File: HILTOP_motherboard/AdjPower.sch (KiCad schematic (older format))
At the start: 92 parts, among them Q1 Q_NMOS_DS_POWERPAK, Q2 Q_NMOS_DS_POWERPAK, Q4 2N7002, U10 TLC271, U11 ADS1015, U12 MCP4725, U8 LM5118, U9 INA250A3

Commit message: Furthe progress on Schematics, assigned all main footprints using latest libraries, removed unwanted tracking and parts from original PCB layout
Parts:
- C111, C115, C184, C185, C193, C194, C63, C64, C69: footprint Capacitors_SMD:C_0805 -> Capacitor_SMD:C_0805_2012Metric
- C112, C117, C118, C180, C187, C188, C189, C190, C191, C192, C57, C60, C61, C62: footprint Capacitors_SMD:C_0603 -> Capacitor_SMD:C_0603_1608Metric
- C179, C56, C58: footprint Capacitors_SMD:C_1206 -> Capacitor_SMD:C_1206_3216Metric
- C181, C182, C183, C65: footprint Capacitors_SMD:C_1210 -> Capacitor_SMD:C_1210_3225Metric
- C186, C67: footprint Capacitors_SMD:CP_Elec_6.3x7.7 -> Capacitor_SMD:CP_Elec_6.3x7.7
- C54: footprint Capacitors_SMD:C_0603 -> Capacitor_SMD:C_0201_0603Metric
- C70, C79: renamed from C?; footprint Capacitors_SMD:CP_Elec_6.3x7.7 -> Capacitor_SMD:CP_Elec_6.3x7.7
- D10, D19, D7, D8, D9, Q4: footprint TO_SOT_Packages_SMD:SOT-23 -> Package_TO_SOT_SMD:SOT-23
- D5: footprint KiCAD_PCB_Lib:TO-263AB -> Devtank_PCB_Lib:TO-263AB
- D6: footprint KiCAD_PCB_Lib:DPAK -> Devtank_PCB_Lib:DPAK
- L4: footprint KiCAD_PCB_Lib:Inductor_Coilcraft_SER2800 -> Devtank_PCB_Lib:Inductor_Coilcraft_SER2800
- Q1, Q2: footprint KiCAD_PCB_Lib:PowerPAK_SO-8 -> Devtank_PCB_Lib:PowerPAK_SO-8
- R105, R112, R113, R114, R115, R116, R117, R118, R123, R132, R133, R142, R143, R165, R166, R57, R58, R59, R60, R61, R62, R64, R74, R75, R76: footprint Resistors_SMD:R_0603 -> Resistor_SMD:R_0603_1608Metric
- R63: footprint Resistors_SMD:R_1206 -> Resistor_SMD:R_1206_3216Metric
- R65, R66, R67, R68: footprint Resistors_SMD:R_0603 -> Resistor_SMD:R_0603_1608Metric_Pad0.84x1.00mm_HandSolder
- R69: footprint KiCAD_PCB_Lib:RL7520W_3008 -> Devtank_PCB_Lib:RL7520W_3008
- RL1: footprint KiCAD_PCB_Lib:Relay_SPST_TE_PCH -> Devtank_PCB_Lib:Relay_SPST_TE_PCH
- TP1, TP2, TP3, TP4, TP5, TP6, TP7: footprint Measurement_Points:Measurement_Point_Round-TH_Small -> TestPoint:TestPoint_THTPad_D1.5mm_Drill0.7mm
- U10: footprint Housings_SOIC:SOIC-8_3.9x4.9mm_Pitch1.27mm -> Package_SOIC:SOIC-8_3.9x4.9mm_P1.27mm
- U11: footprint Housings_SSOP:TSSOP-10_3x3mm_Pitch0.5mm -> Package_SSOP:TSSOP-10_3x3mm_P0.5mm
- U12: footprint TO_SOT_Packages_SMD:SOT-23-6 -> Package_TO_SOT_SMD:SOT-23-6
- U8: footprint Housings_SSOP:HTSSOP-20-1EP_4.4x6.5mm_Pitch0.65mm_ThermalPad -> Package_SSOP:HTSSOP-20-1EP_4.4x6.5mm_P0.65mm_ThermalPad
- U9: footprint Housings_SSOP:TSSOP-16_4.4x5mm_Pitch0.65mm -> Package_SSOP:TSSOP-16_4.4x5mm_P0.65mm
- W1: footprint Measurement_Points:Measurement_Point_Round-TH_Small -> TestPoint:TestPoint_THTPad_1.5x1.5mm_Drill0.7mm

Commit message: Schematics complete - 1st draft
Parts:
- C111, C112, C115, C117, C118, C179, C180, C181, C182, C183, C184, C185, C187, C188, C189, C190, C191, C192, C193, C194, C54, C56, C57, C58, C60, C61, C62, C63, C64, C65, C69: symbol C -> device:C
- C186, C67, C70, C79: symbol CP -> device:CP
- D10, D7, D8, D9: symbol D_x2_Serial_AKC -> device:D_x2_Serial_AKC
- D19: symbol D_Schottky -> device:D_Schottky
- D20: symbol D -> device:D
- D5: symbol D_Schottky_x2_KCom_AAK -> device:D_Schottky_x2_KCom_AAK
- D6: symbol D_Schottky_x2_KCom_AKA -> device:D_Schottky_x2_KCom_AKA
- L4: symbol L -> device:L
- Q1, Q2: symbol Q_NMOS_DS_POWERPAK -> Devtank:Q_NMOS_DS_POWERPAK
- Q4: symbol 2N7002 -> Transistor:2N7002
- R105, R112, R113, R114, R115, R116, R117, R118, R123, R132, R133, R142, R143, R165, R166, R57, R58, R59, R60, R61, R62, R63, R64, R65, R66, R67, R68, R69, R74, R75, R76: symbol R -> device:R
- RL1: symbol SPST-NO -> Devtank:SPST-NO
- TP1, TP2, TP3, TP4, TP5, TP6, TP7: footprint TestPoint:TestPoint_THTPad_D1.5mm_Drill0.7mm -> TestPoint:TestPoint_THTPad_D1.0mm_Drill0.5mm; symbol TEST_1P -> HILTOP_Motherboard-rescue:TEST_1P
- U10: symbol TLC271 -> Devtank:TLC271
- U11: symbol ADS1015 -> Devtank:ADS1015
- U12: symbol MCP4725 -> Devtank:MCP4725
- U8: symbol LM5118 -> Devtank:LM5118
- U9: symbol INA250 -> Devtank:INA250
- W1: symbol TEST_1P -> HILTOP_Motherboard-rescue:TEST_1P
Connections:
- net labels removed: PSU_ADC_ADDR, PSU_ALERT_RDY, PSU_DAC_ADDR
- wire segments 306 -> 418

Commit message: BOM nearly complete!
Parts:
- removed W1: TP, TestPoint:TestPoint_THTPad_1.5x1.5mm_Drill0.7mm, symbol HILTOP_Motherboard-rescue:TEST_1P
- added TP95: TP, TestPoint:TestPoint_THTPad_D1.0mm_Drill0.5mm, symbol HILTOP_Motherboard-rescue:TEST_1P
- Q1, Q2: value Q_NMOS_DS_POWERPAK -> Si7148DP-T1-E3
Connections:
- net at U8.11 (SYNC): now also TP95.1
- no-connect marks 0 -> 3
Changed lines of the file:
@@
 $Descr A3 16535 11693
 encoding utf-8
-Sheet 7 12
+Sheet 6 12
 Title "HILTOP Motherboard"
 Date "26th January 2018"
@@
 $EndComp
 $Comp
-L HILTOP_Motherboard-rescue:TEST_1P W1
-U 1 1 58E90AB1
-P 5550 4850
-F 0 "W1" H 5550 5120 50  0000 C CNN
-F 1 "TP" H 5550 5050 50  0000 C CNN
-F 2 "TestPoint:TestPoint_THTPad_1.5x1.5mm_Drill0.7mm" H 5750 4850 50  0001 C CNN
-F 3 "" H 5750 4850 50  0000 C CNN
-	1    5550 4850
-	-1   0    0    1
-$EndComp
-$Comp
 L device:C C64
 U 1 1 58E9153E
@@
 P 6800 3100
 F 0 "Q1" H 7000 3150 50  0000 L CNN
-F 1 "Q_NMOS_DS_POWERPAK" H 7000 3050 50  0000 L CNN
+F 1 "Si7148DP-T1-E3" H 7000 3050 50  0000 L CNN
 F 2 "Devtank_PCB_Lib:PowerPAK_SO-8" H 7000 3200 50  0001 C CNN
 F 3 "" H 6800 3100 50  0000 C CNN
@@
 P 7350 5000
 F 0 "Q2" H 7550 5050 50  0000 L CNN
-F 1 "Q_NMOS_DS_POWERPAK" H 7550 4950 50  0000 L CNN
+F 1 "Si7148DP-T1-E3" H 7550 4950 50  0000 L CNN
 F 2 "Devtank_PCB_Lib:PowerPAK_SO-8" H 7550 5100 50  0001 C CNN
 F 3 "" H 7350 5000 50  0000 C CNN
@@
 Wire Wire Line
 	9400 6300 9600 6300
+NoConn ~ 15100 4800
+NoConn ~ 8550 8500
+NoConn ~ 8450 8550
+$Comp
+L HILTOP_Motherboard-rescue:TEST_1P TP?
+U 1 1 5CBFAD8E
+P 5550 4850
+AR Path="/5CBFAD8E" Ref="TP?"  Part="1"
+AR Path="/589A1BA0/5CBFAD8E" Ref="TP95"  Part="1"
+F 0 "TP95" H 5550 5100 50  0000 C CNN
+F 1 "TP" H 5550 5050 50  0001 C CNN
+F 2 "TestPoint:TestPoint_THTPad_D1.0mm_Drill0.5mm" H 5750 4850 50  0001 C CNN
+F 3 "" H 5750 4850 50  0000 C CNN
+	1    5550 4850
+	-1   0    0    1
+$EndComp
 $EndSCHEMATC

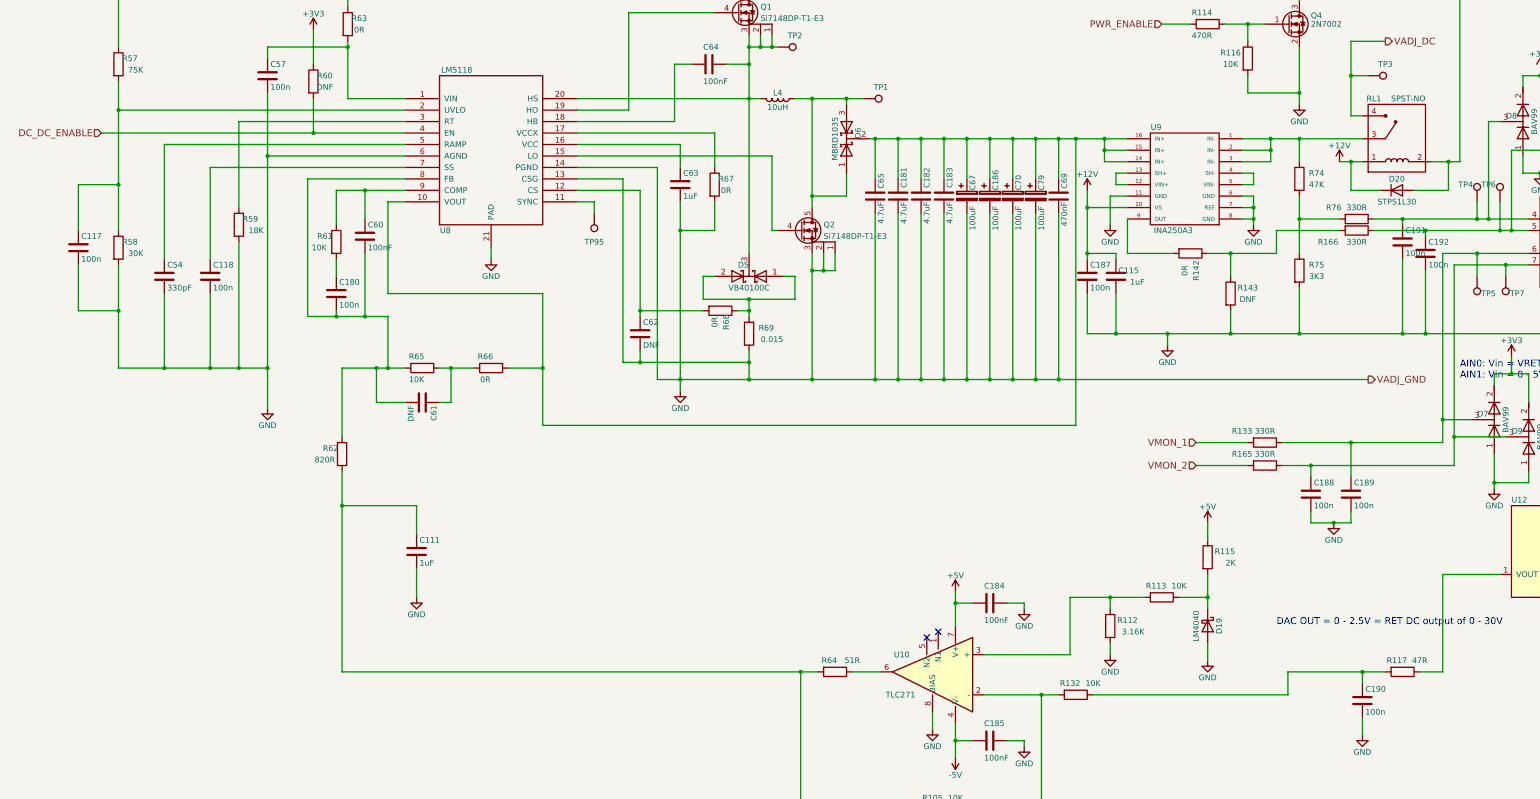
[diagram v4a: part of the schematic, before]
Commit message: DRC checks complete, all errors and warnings cleared. BOM created and parts rationalised.
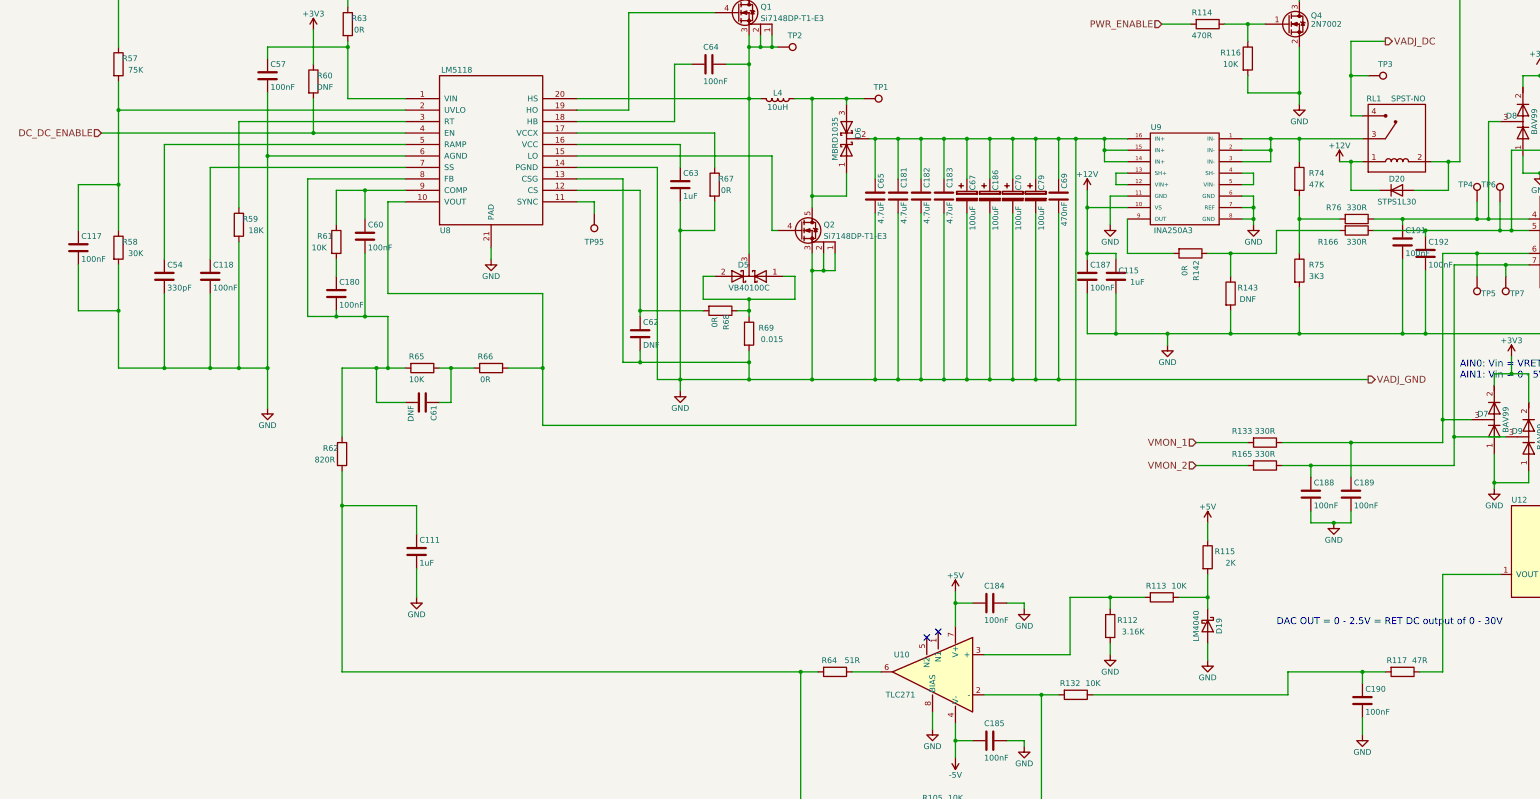
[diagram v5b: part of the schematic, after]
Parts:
- C117, C118, C180, C187, C188, C189, C190, C191, C192, C57: value 100n -> 100nF
- C184, C185, C193, C194, C64: footprint Capacitor_SMD:C_0805_2012Metric -> Capacitor_SMD:C_0603_1608Metric
- C54: footprint Capacitor_SMD:C_0201_0603Metric -> Capacitor_SMD:C_0402_1005Metric
- R65, R66, R67, R68: footprint Resistor_SMD:R_0603_1608Metric_Pad0.84x1.00mm_HandSolder -> Resistor_SMD:R_0603_1608Metric
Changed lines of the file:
@@
 P 2700 3650
 F 0 "C57" H 2725 3750 50  0000 L CNN
-F 1 "100n" H 2725 3550 50  0000 L CNN
+F 1 "100nF" H 2725 3550 50  0000 L CNN
 F 2 "Capacitor_SMD:C_0603_1608Metric" H 2738 3500 50  0001 C CNN
 F 3 "" H 2700 3650 50  0000 C CNN
@@
 F 0 "R65" V 3950 6150 50  0000 C CNN
 F 1 "10K" V 4150 6150 50  0000 C CNN
-F 2 "Resistor_SMD:R_0603_1608Metric_Pad0.84x1.00mm_HandSolder" V 3980 6200 50  0001 C CNN
+F 2 "Resistor_SMD:R_0603_1608Metric" V 3980 6200 50  0001 C CNN
 F 3 "" H 4050 6200 50  0000 C CNN
 F 4 "101-010" V 4050 6200 60  0001 C CNN "Devtank"
@@
 F 0 "R66" V 4550 6150 50  0000 C CNN
 F 1 "0R" V 4750 6150 50  0000 C CNN
-F 2 "Resistor_SMD:R_0603_1608Metric_Pad0.84x1.00mm_HandSolder" V 4580 6200 50  0001 C CNN
+F 2 "Resistor_SMD:R_0603_1608Metric" V 4580 6200 50  0001 C CNN
 F 3 "" H 4650 6200 50  0000 C CNN
 F 4 "101-005" V 4650 6200 60  0001 C CNN "Devtank"
@@
 F 0 "C54" H 1825 5500 50  0000 L CNN
 F 1 "330pF" H 1825 5300 50  0000 L CNN
-F 2 "Capacitor_SMD:C_0201_0603Metric" H 1838 5250 50  0001 C CNN
+F 2 "Capacitor_SMD:C_0402_1005Metric" H 1838 5250 50  0001 C CNN
 F 3 "" H 1800 5400 50  0000 C CNN
 F 4 "106-001" H 1800 5400 60  0001 C CNN "Devtank"
@@
 F 0 "R67" H 6700 4650 50  0000 C CNN
 F 1 "0R" H 6700 4550 50  0000 C CNN
-F 2 "Resistor_SMD:R_0603_1608Metric_Pad0.84x1.00mm_HandSolder" V 6530 4600 50  0001 C CNN
+F 2 "Resistor_SMD:R_0603_1608Metric" V 6530 4600 50  0001 C CNN
 F 3 "" H 6600 4600 50  0000 C CNN
 F 4 "101-005" H 6600 4600 60  0001 C CNN "Devtank"
@@
 F 0 "R68" H 6750 5750 50  0000 C CNN
 F 1 "0R" H 6750 5650 50  0000 C CNN
-F 2 "Resistor_SMD:R_0603_1608Metric_Pad0.84x1.00mm_HandSolder" V 6580 5700 50  0001 C CNN
+F 2 "Resistor_SMD:R_0603_1608Metric" V 6580 5700 50  0001 C CNN
 F 3 "" H 6650 5700 50  0000 C CNN
 F 4 "101-005" H 6650 5700 60  0001 C CNN "Devtank"
@@
 F 0 "C64" V 6400 3500 50  0000 L CNN
 F 1 "100nF" V 6700 3500 50  0000 L CNN
-F 2 "Capacitor_SMD:C_0805_2012Metric" H 6588 3400 50  0001 C CNN
+F 2 "Capacitor_SMD:C_0603_1608Metric" H 6588 3400 50  0001 C CNN
 F 3 "" H 6550 3550 50  0000 C CNN
 F 4 "105-002" V 6550 3550 60  0001 C CNN "Devtank"
@@
 P 2200 5400
 F 0 "C118" H 2225 5500 50  0000 L CNN
-F 1 "100n" H 2225 5300 50  0000 L CNN
+F 1 "100nF" H 2225 5300 50  0000 L CNN
 F 2 "Capacitor_SMD:C_0603_1608Metric" H 2238 5250 50  0001 C CNN
 F 3 "" H 2200 5400 50  0000 C CNN
@@
 P 1050 5150
 F 0 "C117" H 1075 5250 50  0000 L CNN
-F 1 "100n" H 1075 5050 50  0000 L CNN
+F 1 "100nF" H 1075 5050 50  0000 L CNN
 F 2 "Capacitor_SMD:C_0603_1608Metric" H 1088 5000 50  0001 C CNN
 F 3 "" H 1050 5150 50  0000 C CNN
@@
 P 3300 5550
 F 0 "C180" H 3325 5650 50  0000 L CNN
-F 1 "100n" H 3325 5450 50  0000 L CNN
+F 1 "100nF" H 3325 5450 50  0000 L CNN
 F 2 "Capacitor_SMD:C_0603_1608Metric" H 3338 5400 50  0001 C CNN
 F 3 "" H 3300 5550 50  0000 C CNN
@@
 F 0 "C194" V 14500 4250 50  0000 L CNN
 F 1 "100nF" V 14800 4250 50  0000 L CNN
-F 2 "Capacitor_SMD:C_0805_2012Metric" H 14688 4150 50  0001 C CNN
+F 2 "Capacitor_SMD:C_0603_1608Metric" H 14688 4150 50  0001 C CNN
 F 3 "" H 14650 4300 50  0000 C CNN
 F 4 "105-002" V 14650 4300 60  0001 C CNN "Devtank"
@@
 P 9850 5400
 F 0 "C187" H 9875 5500 50  0000 L CNN
-F 1 "100n" H 9875 5300 50  0000 L CNN
+F 1 "100nF" H 9875 5300 50  0000 L CNN
 F 2 "Capacitor_SMD:C_0603_1608Metric" H 9888 5250 50  0001 C CNN
 F 3 "" H 9850 5400 50  0000 C CNN
@@
 P 12600 5100
 F 0 "C191" H 12625 5200 50  0000 L CNN
-F 1 "100n" H 12625 5000 50  0000 L CNN
+F 1 "100nF" H 12625 5000 50  0000 L CNN
 F 2 "Capacitor_SMD:C_0603_1608Metric" H 12638 4950 50  0001 C CNN
 F 3 "" H 12600 5100 50  0000 C CNN
@@
 P 12800 5200
 F 0 "C192" H 12825 5300 50  0000 L CNN
-F 1 "100n" H 12825 5100 50  0000 L CNN
+F 1 "100nF" H 12825 5100 50  0000 L CNN
 F 2 "Capacitor_SMD:C_0603_1608Metric" H 12838 5050 50  0001 C CNN
 F 3 "" H 12800 5200 50  0000 C CNN
@@
 P 11800 7300
 F 0 "C188" H 11825 7400 50  0000 L CNN
-F 1 "100n" H 11825 7200 50  0000 L CNN
+F 1 "100nF" H 11825 7200 50  0000 L CNN
 F 2 "Capacitor_SMD:C_0603_1608Metric" H 11838 7150 50  0001 C CNN
 F 3 "" H 11800 7300 50  0000 C CNN
@@
 P 12150 7300
 F 0 "C189" H 12175 7400 50  0000 L CNN
-F 1 "100n" H 12175 7200 50  0000 L CNN
+F 1 "100nF" H 12175 7200 50  0000 L CNN
 F 2 "Capacitor_SMD:C_0603_1608Metric" H 12188 7150 50  0001 C CNN
 F 3 "" H 12150 7300 50  0000 C CNN
@@
 F 0 "C193" V 14100 6950 50  0000 L CNN
 F 1 "100nF" V 14400 6950 50  0000 L CNN
-F 2 "Capacitor_SMD:C_0805_2012Metric" H 14288 6850 50  0001 C CNN
+F 2 "Capacitor_SMD:C_0603_1608Metric" H 14288 6850 50  0001 C CNN
 F 3 "" H 14250 7000 50  0000 C CNN
 F 4 "105-002" V 14250 7000 60  0001 C CNN "Devtank"
@@
 P 12250 9100
 F 0 "C190" H 12275 9200 50  0000 L CNN
-F 1 "100n" H 12275 9000 50  0000 L CNN
+F 1 "100nF" H 12275 9000 50  0000 L CNN
 F 2 "Capacitor_SMD:C_0603_1608Metric" H 12288 8950 50  0001 C CNN
 F 3 "" H 12250 9100 50  0000 C CNN
@@
 F 0 "C184" V 8850 8200 50  0000 L CNN
 F 1 "100nF" V 9150 8200 50  0000 L CNN
-F 2 "Capacitor_SMD:C_0805_2012Metric" H 9038 8100 50  0001 C CNN
+F 2 "Capacitor_SMD:C_0603_1608Metric" H 9038 8100 50  0001 C CNN
 F 3 "" H 9000 8250 50  0000 C CNN
 F 4 "105-002" V 9000 8250 60  0001 C CNN "Devtank"
@@
 F 0 "C185" V 8850 9400 50  0000 L CNN
 F 1 "100nF" V 9150 9400 50  0000 L CNN
-F 2 "Capacitor_SMD:C_0805_2012Metric" H 9038 9300 50  0001 C CNN
+F 2 "Capacitor_SMD:C_0603_1608Metric" H 9038 9300 50  0001 C CNN
 F 3 "" H 9000 9450 50  0000 C CNN
 F 4 "105-002" V 9000 9450 60  0001 C CNN "Devtank"

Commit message: Rev C - pre-release
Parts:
- C111, C112, C115, C117, C118, C179, C180, C181, C182, C183, C184, C185, C187, C188, C189, C190, C191, C192, C193, C194, C54, C56, C57, C58, C60, C61, C62, C63, C64, C65, C69: symbol device:C -> HILTOP_Motherboard-rescue:C-device
- C186, C67, C70, C79: symbol device:CP -> HILTOP_Motherboard-rescue:CP-device
- D10, D7, D8, D9: symbol device:D_x2_Serial_AKC -> HILTOP_Motherboard-rescue:D_x2_Serial_AKC-device
- D19: symbol device:D_Schottky -> HILTOP_Motherboard-rescue:D_Schottky-device
- D20: symbol device:D -> HILTOP_Motherboard-rescue:D-device
- D5: symbol device:D_Schottky_x2_KCom_AAK -> HILTOP_Motherboard-rescue:D_Schottky_x2_KCom_AAK-device
- D6: symbol device:D_Schottky_x2_KCom_AKA -> HILTOP_Motherboard-rescue:D_Schottky_x2_KCom_AKA-device
- L4: symbol device:L -> HILTOP_Motherboard-rescue:L-device
- Q4: symbol Transistor:2N7002 -> HILTOP_Motherboard-rescue:2N7002-Transistor
- R105, R112, R113, R114, R115, R116, R117, R118, R123, R132, R133, R142, R143, R165, R166, R57, R58, R59, R60, R61, R62, R63, R64, R65, R66, R67, R68, R69, R74, R75, R76: symbol device:R -> HILTOP_Motherboard-rescue:R-device
